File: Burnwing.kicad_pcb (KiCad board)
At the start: 2 copper layers, 54 x 22.9 mm, 43 parts, among them J1 Conn_01x06_MountingPin, J2 Molex_PicoBlade_53398-0471_1x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, J3 feather long, J4 feather short, Q1 AO3400A, U1 BTS3405GXUMA1, U1 NCV8402ADDR2G

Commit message: initial commit
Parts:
- removed +, -: SolderWirePad_1x01_SMD_1x2mm, Connector_Wire:SolderWirePad_1x01_SMD_1x2mm
- removed D4, D5: D_SOD-123F, Diode_SMD:D_SOD-123F
- removed Q1: AO3400A, Package_TO_SOT_SMD:SOT-23_Handsoldering
- removed R11: 5k1, Resistor_SMD:R_0603_1608Metric_Pad0.98x0.95mm_HandSolder
- removed the R5 at (99.3, 94.5)
- removed the R6 at (103.9, 94.5)
- added REF**: 21-0041B_8_MXM, Library:DS3231MZ_TRL-L, F.Cu at (118.5, 74.1)
- added S2: Tactile_Button, 00-footprint-lib:SW-SMD_4P-L5.1-W5.1-P3.70-LS6.5-TL-2, F.Cu at (98.7, 91.2)
- added S2: Tactile_Button, 00-footprint-lib:SW-SMD_4P-L5.1-W5.1-P3.70-LS6.5-TL-2, F.Cu at (92.3, 91.2)
- moved C2 29.6 mm to (62.9, 88.1)
- moved C3 29.6 mm to (56.7, 91.5)
- moved C4 29.6 mm to (58.2, 91.5)
- moved L1 29.6 mm to (61.3, 92.2)
- moved R1 29.6 mm to (55.2, 86.6)
- moved R2 29.6 mm to (55.2, 91.5)
- moved R7 29.6 mm to (55.2, 83.1)
- moved U1 29.6 mm to (60.5, 87.0)
- moved C1 29.6 mm to (57.6, 87.2)
- moved J1 28.5 mm to (92.8, 65.8), turned to 180 degrees
- moved D2 24.3 mm to (118.9, 105.5)
- moved D1 24.3 mm to (114.3, 105.5)
- moved R3 24.3 mm to (116.1, 105.7)
- moved R4 24.3 mm to (120.7, 105.7)
- moved Burn 1 23.1 mm to (80.4, 109.4)
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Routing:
- net GND: track 53.0 -> 3.05 mm, vias 28 -> 8
- net Vin: track 29.9 -> 1.69 mm
- net BURN_CTRL_1: track 36.0 -> 13.7 mm
- net EN3V: track 28.7 -> 7.30 mm, vias 3 -> 2
- net /Burn_Circuit/BURN_OUT_NEG: track 15.8 -> 9.24 mm
- net Net-(H3-Pad1): track 4.11 -> 0.00 mm
- net Net-(H4-Pad1): track 4.10 -> 0.00 mm
- net (no net): track 7.68 -> 3.86 mm
- net BURN_CTRL_2: track 18.6 -> 14.8 mm, vias 1 -> 0
- net Net-(H1-Pad1): track 3.59 -> 0.00 mm
- net +5V: track 2.25 -> 0.00 mm
- net IN2: track 1.92 -> 0.00 mm
- net IN1: track 1.88 -> 0.00 mm
- net /Burn_Circuit1/BURN_OUT_NEG: track 17.5 -> 15.8 mm
- removed copper zone on F.Cu, net +5V
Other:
- board size 54 x 22.9 mm -> 50.8 x 22.9 mm
- board text removed: "A4"
- board text removed: "A5"
- board text removed: "B3"
- board text removed: "B4"
- board text removed: "B5"
- board text removed: "MISO"
- board text removed: "MOSI"
- board text removed: "RX"
- board text removed: "SCK"
- board text removed: "TX"

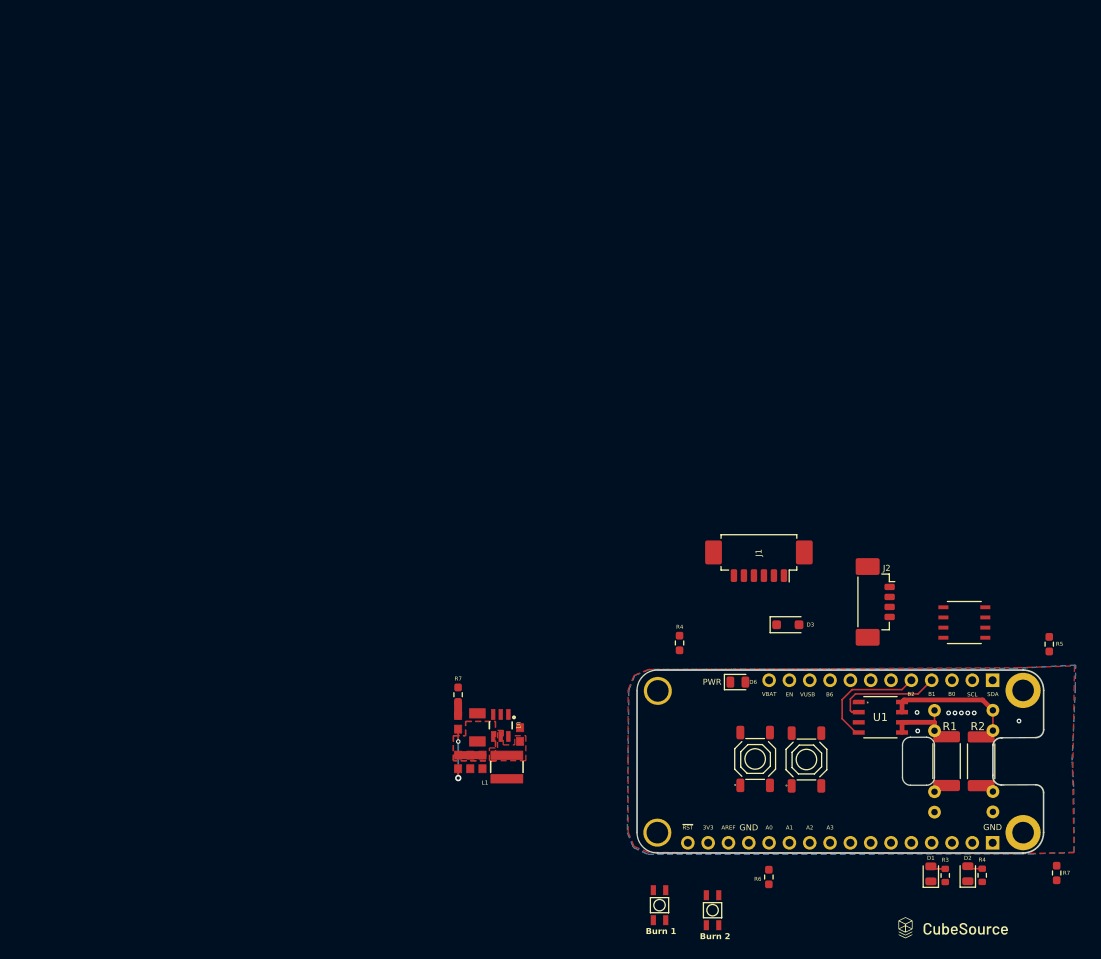
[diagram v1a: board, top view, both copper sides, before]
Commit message: Changed to USB C power
Switched our regulator for selectable usb C power delivery
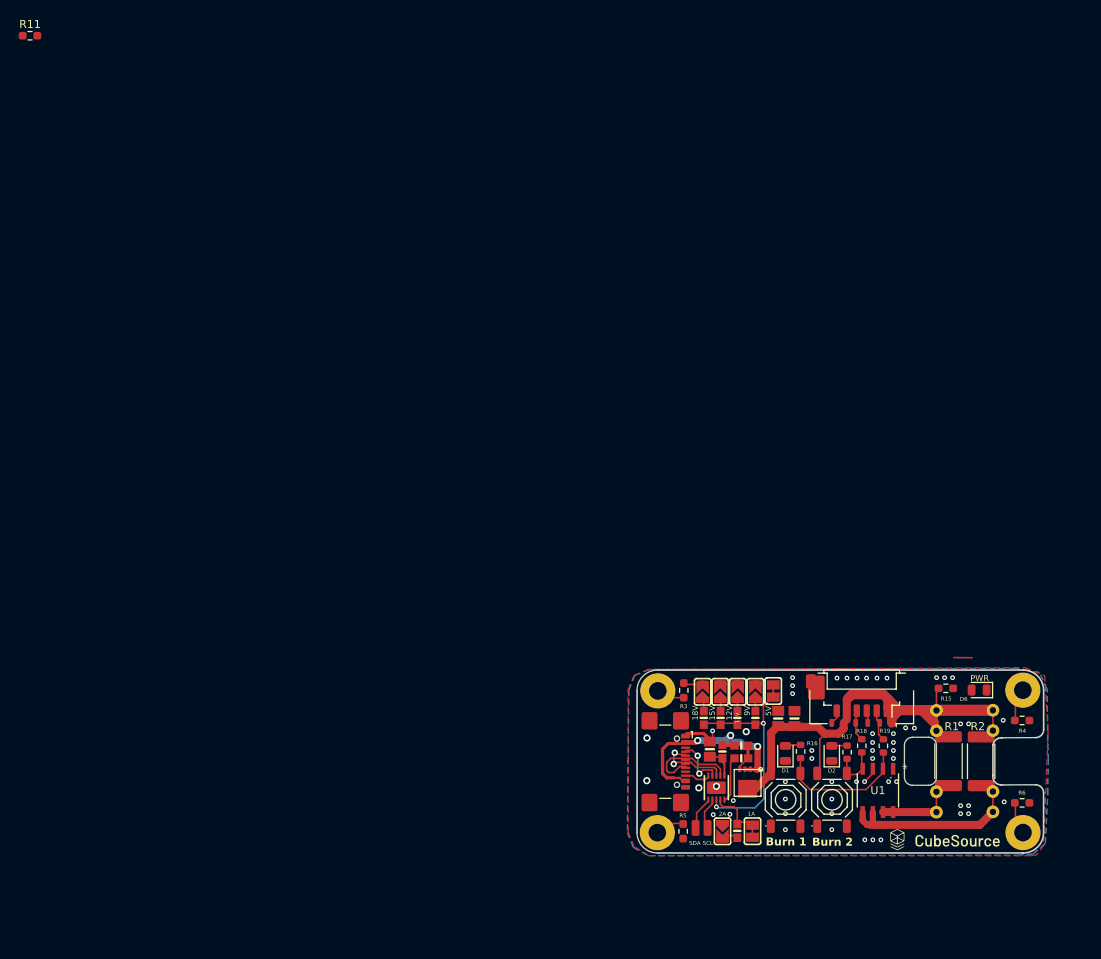
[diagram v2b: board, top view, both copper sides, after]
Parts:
- removed the Burn 1 at (80.4, 109.4)
- removed the Burn 2 at (87.0, 110.1)
- removed C1: 10uF, 1210
- removed D3: D_SOD-123F, Diode_SMD:D_SOD-123F
- removed the H3 at (125.8, 100.4)
- removed the H3 at (125.8, 82.6)
- removed J2: Molex_PicoBlade_53398-0471_1x04-1MP_P1.25mm_Vertical, Connector_Molex:Molex_PicoBlade_53398-0471_1x04-1MP_P1.25mm_Vertical
- removed J3: feather long, Connector_PinHeader_2.54mm:PinHeader_1x16_P2.54mm_Vertical
- removed J4: feather short, Connector_PinHeader_2.54mm:PinHeader_1x12_P2.54mm_Vertical
- removed L1: 4.7uH, INDUCTOR_4X4MM
- removed the R1 at (55.2, 86.6)
- removed the R2 at (55.2, 91.5)
- removed the REF** at (118.5, 74.1)
- removed the U1 at (60.5, 87.0)
- added 12V: 10K, Adafruit HUSB238 USB-C PD Breakout:0603-NO, F.Cu at (90.1, 86.0)
- added 15V: 14K, Adafruit HUSB238 USB-C PD Breakout:0603-NO, F.Cu at (88.0, 86.0)
- added 18V: 18K, Adafruit HUSB238 USB-C PD Breakout:0603-NO, F.Cu at (85.9, 86.0)
- added 1A: , Adafruit HUSB238 USB-C PD Breakout:SOLDERJUMPER_CLOSEDWIRE, F.Cu at (92.0, 100.2)
- added 2A: , Adafruit HUSB238 USB-C PD Breakout:SOLDERJUMPER_ARROW_NOPASTE, F.Cu at (88.2, 100.2)
- added 5V: , Adafruit HUSB238 USB-C PD Breakout:SOLDERJUMPER_CLOSEDWIRE, F.Cu at (94.6, 82.7)
- added 9V: 6K, Adafruit HUSB238 USB-C PD Breakout:0603-NO, F.Cu at (92.3, 86.0)
- added H2: MountingHole_Pad, MountingHole:MountingHole_2.2mm_M2_Pad, F.Cu at (125.8, 82.6)
- added H4: MountingHole_Pad, MountingHole:MountingHole_2.2mm_M2_Pad, F.Cu at (125.8, 100.4)
- added PLABEL0: , Adafruit HUSB238 USB-C PD Breakout:PLABEL0, F.Cu at (99.5, 96.2)
- added PLABEL1: , Adafruit HUSB238 USB-C PD Breakout:PLABEL1, F.Cu at (89.7, 106.1)
- added PLABEL10: , Adafruit HUSB238 USB-C PD Breakout:PLABEL10, F.Cu at (95.5, 86.2)
- added PLABEL12: , Adafruit HUSB238 USB-C PD Breakout:PLABEL12, F.Cu at (89.5, 97.2)
- added PLABEL13: , Adafruit HUSB238 USB-C PD Breakout:PLABEL13, F.Cu at (85.2, 97.2)
- added PLABEL14: , Adafruit HUSB238 USB-C PD Breakout:PLABEL14, F.Cu at (83.0, 97.2)
- added PLABEL15: , Adafruit HUSB238 USB-C PD Breakout:PLABEL15, F.Cu at (82.8, 99.5)
- added PLABEL16: , Adafruit HUSB238 USB-C PD Breakout:PLABEL16, F.Cu at (99.5, 93.8)
- added PLABEL17: , Adafruit HUSB238 USB-C PD Breakout:PLABEL17, F.Cu at (101.6, 89.0)
- added PLABEL18: , Adafruit HUSB238 USB-C PD Breakout:PLABEL18, B.Cu at (81.0, 91.3)
- added PLABEL19: , Adafruit HUSB238 USB-C PD Breakout:PLABEL19, B.Cu at (88.8, 91.3)
- added PLABEL2: , Adafruit HUSB238 USB-C PD Breakout:PLABEL2, F.Cu at (92.2, 108.7)
- added PLABEL3: , Adafruit HUSB238 USB-C PD Breakout:PLABEL3, F.Cu at (99.5, 98.8)
- added PLABEL4: , Adafruit HUSB238 USB-C PD Breakout:PLABEL4, F.Cu at (85.1, 91.7)
- added PLABEL8: , Adafruit HUSB238 USB-C PD Breakout:PLABEL8, F.Cu at (91.6, 86.2)
- added PLABEL9: , Adafruit HUSB238 USB-C PD Breakout:PLABEL9, F.Cu at (94.0, 86.2)
- added Q1: AONR21307, Adafruit HUSB238 USB-C PD Breakout:POWERDI3333, F.Cu at (91.4, 93.9)
- added R11: 6K, Resistor_SMD:R_0603_1608Metric_Pad0.98x0.95mm_HandSolder, F.Cu at (1.68, 0.76)
- added R15: 6K, Resistor_SMD:R_0603_1608Metric_Pad0.98x0.95mm_HandSolder, F.Cu at (116.2, 82.3)
- added R18: 5.1K, Resistor_SMD:R_0603_1608Metric, F.Cu at (105.7, 89.5)
- added R19: 14K, Resistor_SMD:R_0603_1608Metric, F.Cu at (108.3, 89.5)
- added R8: 49.9K, Adafruit HUSB238 USB-C PD Breakout:0603-NO, F.Cu at (90.1, 100.1)
- added R8: 49.9K, Adafruit HUSB238 USB-C PD Breakout:0603-NO, F.Cu at (90.6, 89.5)
- added R9: 5.1K, Adafruit HUSB238 USB-C PD Breakout:0603-NO, F.Cu at (90.6, 91.1)
- added SCL: SolderWirePad_1x01_SMD_1x2mm, Library:SolderWirePad_1x01_SMD_1x2mm, F.Cu at (86.4, 99.8)
- added SDA: SolderWirePad_1x01_SMD_1x2mm, Library:SolderWirePad_1x01_SMD_1x2mm, F.Cu at (84.9, 99.8)
- added SJ2: SOLDERJUMPER, Adafruit HUSB238 USB-C PD Breakout:SOLDERJUMPER_ARROW_NOPASTE, F.Cu at (92.3, 82.8)
- added SJ3: SOLDERJUMPER, Adafruit HUSB238 USB-C PD Breakout:SOLDERJUMPER_ARROW_NOPASTE, F.Cu at (90.2, 82.8)
- added SJ4: SOLDERJUMPER, Adafruit HUSB238 USB-C PD Breakout:SOLDERJUMPER_ARROW_NOPASTE, F.Cu at (88.0, 82.8)
- added SJ5: SOLDERJUMPER, Adafruit HUSB238 USB-C PD Breakout:SOLDERJUMPER_ARROW_NOPASTE, F.Cu at (85.8, 82.8)
- added X1: USB_C_Receptacle_GCT_USB4110, Connector_USB:USB_C_Receptacle_GCT_USB4110, F.Cu at (79.9, 91.5)
- added X3: HUSB238, Adafruit HUSB238 USB-C PD Breakout:DFN10_3X3MM, F.Cu at (87.5, 94.8)
- added p: Molex_Pico-Lock_504050-0691_1x06-1MP_P1.50mm_Horizontal, Connector_Molex:Molex_Pico-Lock_504050-0691_1x06-1MP_P1.50mm_Horizontal, F.Cu at (105.6, 83.9)
- Burn 1: renamed from S2
- Burn 2: renamed from S2
- C2: value 0.1uF -> 100n; footprint 0603 -> Adafruit HUSB238 USB-C PD Breakout:0805-NO
- C3: value 0.1uF -> 1uF/50V; footprint 0603 -> Adafruit HUSB238 USB-C PD Breakout:0805-NO
- C4: value 22uF -> 4.7uF; footprint 0603 -> Adafruit HUSB238 USB-C PD Breakout:0805-NO
- G***: footprint LOGO -> Library:LOGO
- R1: value R -> 4.7
- R16: renamed from R3; value 10 -> 10 ohm
- R17: renamed from R4; value 10 -> 49.9K
- R2: value AxialBurnResistor_No_Cutout -> 4.7
- R7: value 0 -> 10 ohm; footprint Resistor_SMD:R_0603_1608Metric_Pad0.98x0.95mm_HandSolder -> Adafruit HUSB238 USB-C PD Breakout:0603-NO
- moved C4 39.4 mm to (97.2, 86.1)
- moved R7 33.8 mm to (88.2, 90.2), turned to 90 degrees
- moved C2 32.3 mm to (95.2, 86.1), turned to 90 degrees
- moved D6 30.2 mm to (120.3, 82.5), turned to 180 degrees
- moved C3 30.0 mm to (86.7, 89.9)
- moved R16 23.8 mm to (98.0, 90.2)
- moved D1 23.6 mm to (96.1, 90.5)
- moved R17 22.8 mm to (103.8, 90.3)
- moved D2 22.7 mm to (101.9, 90.5)
- moved J1 21.2 mm to (105.6, 82.7)
- moved R5 12.1 mm to (83.3, 100.2)
- moved G*** 11.1 mm to (116.0, 101.3)
- moved Burn 2 10.9 mm to (101.9, 96.3)
- moved R4 10.1 mm to (125.7, 86.3), turned to 0 degrees
- moved R6 9.77 mm to (125.7, 96.6), turned to 0 degrees
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- renumbered R4 to R3, R5 to R4, R6 to R5, R7 to R6
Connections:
- Burn 1 pad 1: (no net) -> VOUT
- Burn 1 pad 2: (no net) -> VOUT
- Burn 1 pad 3: (no net) -> BURN_CTRL_1
- Burn 1 pad 4: (no net) -> BURN_CTRL_1
- Burn 2 pad 1: (no net) -> VOUT
- Burn 2 pad 2: (no net) -> VOUT
- Burn 2 pad 3: (no net) -> BURN_CTRL_1
- Burn 2 pad 4: (no net) -> BURN_CTRL_2
- C2 pad 1: (no net) -> VDC
- C2 pad 2: Vin -> GND
- C3 pad 1: +5V -> Net-(X3-VIN)
- C4 pad 1: +5V -> /VOUT
- D6 pad 2: Vin -> (no net)
- J1 pad 1: Vin -> VOUT
- J1 pad 2: Vin -> BURN_CTRL_1
- J1 pad 3: Vin -> GND
- J1 pad 4: GND -> BURN_CTRL_2
- J1 pad 5: GND -> VOUT
- R1 pad 1: /Burn_Circuit/BURN_OUT_NEG -> unconnected-(R1-Pad1)
- R1 pad 2: +5V -> Net-(R1-Pad2)
- R16 pad 1: IN1 -> Net-(X3-VIN)
- R16 pad 2: (no net) -> Net-(Q1-S-Pad1)
- R17 pad 1: IN2 -> Net-(Q1-S-Pad1)
- R17 pad 2: (no net) -> Net-(Q1-G)
- R2 pad 1: /Burn_Circuit1/BURN_OUT_NEG -> unconnected-(R2-Pad1)
- R2 pad 2: +5V -> Net-(R2-Pad2)
- R4 pad 1: (no net) -> Net-(H2-Pad1)
- R5 pad 1: GND -> Net-(H3-Pad1)
- R5 pad 2: Net-(H3-Pad1) -> GND
- R7 pad 1: Vin -> Net-(X3-VIN)
- R7 pad 2: Vin -> Net-(Q1-S-Pad1)
- REF** pad 1: /Burn_Circuit1/BURN_OUT_NEG -> VOUT
- REF** pad 2: +5V -> Net-(R2-Pad2)
- REF** pad 1: /Burn_Circuit/BURN_OUT_NEG -> VOUT
- REF** pad 2: +5V -> Net-(R1-Pad2)
- U1 pad 1: GND -> unconnected-(U1-SOURCE1-Pad1)
- U1 pad 2: BURN_CTRL_1 -> /GATE1
- U1 pad 3: GND -> unconnected-(U1-SOURCE2-Pad3)
- U1 pad 4: BURN_CTRL_2 -> /GATE2
- U1 pad 5: /Burn_Circuit/BURN_OUT_NEG -> Net-(R2-Pad2)
- U1 pad 6: /Burn_Circuit/BURN_OUT_NEG -> Net-(R2-Pad2)
- U1 pad 7: /Burn_Circuit1/BURN_OUT_NEG -> Net-(R1-Pad2)
- U1 pad 8: /Burn_Circuit1/BURN_OUT_NEG -> Net-(R1-Pad2)
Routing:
- net VOUT: track 0.00 -> 78.6 mm
- net Net-(Q1-S-Pad1): track 0.00 -> 30.5 mm, vias 0 -> 2
- net N$3: track 0.00 -> 27.9 mm, vias 0 -> 2
- net Net-(R2-Pad2): track 0.00 -> 22.5 mm
- net /Burn_Circuit1/BURN_OUT_NEG: track 15.8 -> 0.00 mm
- net /D+: track 0.00 -> 12.3 mm
- net GND: track 3.05 -> 13.5 mm, vias 8 -> 56
- net /D-: track 0.00 -> 9.69 mm, vias 0 -> 2
- net /Burn_Circuit/BURN_OUT_NEG: track 9.24 -> 0.00 mm
- net Net-(R1-Pad2): track 0.00 -> 9.01 mm
- net EN3V: track 7.30 -> 0.00 mm, vias 2 -> 0
- net BURN_CTRL_1: track 13.7 -> 21.0 mm
- net /CC1: track 0.00 -> 6.75 mm, vias 0 -> 2
- net N$9: track 0.00 -> 6.19 mm
- net Net-(X3-GATE): track 0.00 -> 5.83 mm
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- removed copper zone on F.Cu, net Vin
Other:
- board text removed: "3V3"
- board text removed: "A0"
- board text removed: "A1"
- board text removed: "A2"
- board text removed: "A3"
- board text removed: "AREF"
- board text removed: "B0"
- board text removed: "B1"
- board text removed: "B2"
- board text removed: "B6"
- board text removed: "EN"
- board text removed: "GND"
- board text removed: "SCL"
- board text removed: "SDA"
- board text removed: "VBAT"
- board text removed: "VUSB"
- board text removed: "~{RST}"

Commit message: updated layou/schematic
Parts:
- removed the 12V at (90.1, 86.0)
- removed the 15V at (88.0, 86.0)
- removed the 18V at (85.9, 86.0)
- removed 1A: , Adafruit HUSB238 USB-C PD Breakout:SOLDERJUMPER_CLOSEDWIRE
- removed 2A: , Adafruit HUSB238 USB-C PD Breakout:SOLDERJUMPER_ARROW_NOPASTE
- removed the 9V at (92.3, 86.0)
- removed PLABEL1: , Adafruit HUSB238 USB-C PD Breakout:PLABEL1
- removed PLABEL12: , Adafruit HUSB238 USB-C PD Breakout:PLABEL12
- removed PLABEL13: , Adafruit HUSB238 USB-C PD Breakout:PLABEL13
- removed PLABEL15: , Adafruit HUSB238 USB-C PD Breakout:PLABEL15
- removed PLABEL19: , Adafruit HUSB238 USB-C PD Breakout:PLABEL19
- removed PLABEL2: , Adafruit HUSB238 USB-C PD Breakout:PLABEL2
- removed R11: 6K, Resistor_SMD:R_0603_1608Metric_Pad0.98x0.95mm_HandSolder
- removed R18: 5.1K, Resistor_SMD:R_0603_1608Metric
- removed R19: 14K, Resistor_SMD:R_0603_1608Metric
- removed the R8 at (90.1, 100.1)
- removed the R8 at (90.6, 89.5)
- removed R9: 5.1K, Adafruit HUSB238 USB-C PD Breakout:0603-NO
- removed SCL, SDA: SolderWirePad_1x01_SMD_1x2mm, Library:SolderWirePad_1x01_SMD_1x2mm
- removed SJ2, SJ3, SJ4, SJ5: SOLDERJUMPER, Adafruit HUSB238 USB-C PD Breakout:SOLDERJUMPER_ARROW_NOPASTE
- added 12V: , Adafruit HUSB238 USB-C PD Breakout:SOLDERJUMPER_ARROW_NOPASTE, F.Cu at (88.5, 82.8)
- added 15V: , Adafruit HUSB238 USB-C PD Breakout:SOLDERJUMPER_ARROW_NOPASTE, F.Cu at (86.2, 82.8)
- added 18V: , Adafruit HUSB238 USB-C PD Breakout:SOLDERJUMPER_ARROW_NOPASTE, F.Cu at (84.0, 82.8)
- added 9V: , Adafruit HUSB238 USB-C PD Breakout:SOLDERJUMPER_ARROW_NOPASTE, F.Cu at (90.7, 82.8)
- added C1: 1uF/50V, Adafruit HUSB238 USB-C PD Breakout:0805-NO, F.Cu at (86.8, 90.1)
- added PLABEL11: , Adafruit HUSB238 USB-C PD Breakout:PLABEL11, F.Cu at (87.3, 91.0)
- added PLABEL5: , Adafruit HUSB238 USB-C PD Breakout:PLABEL5, F.Cu at (84.1, 85.0)
- added PLABEL6: , Adafruit HUSB238 USB-C PD Breakout:PLABEL6, F.Cu at (86.5, 85.1)
- added PLABEL7: , Adafruit HUSB238 USB-C PD Breakout:PLABEL7, F.Cu at (88.8, 85.5)
- added R1: 6K, Adafruit HUSB238 USB-C PD Breakout:0603-NO, F.Cu at (91.3, 86.2)
- added R2: 10K, Adafruit HUSB238 USB-C PD Breakout:0603-NO, F.Cu at (89.3, 86.2)
- added R4: 5.1K, Adafruit HUSB238 USB-C PD Breakout:0603-NO, F.Cu at (90.0, 93.7)
- added R6: 14K, Adafruit HUSB238 USB-C PD Breakout:0603-NO, F.Cu at (87.3, 86.2)
- added R8: 14K, Adafruit HUSB238 USB-C PD Breakout:0603-NO, F.Cu at (86.6, 100.0)
- added SJ6: , Adafruit HUSB238 USB-C PD Breakout:SOLDERJUMPER_CLOSEDWIRE, F.Cu at (88.5, 99.9)
- added SJ7: , Adafruit HUSB238 USB-C PD Breakout:SOLDERJUMPER_ARROW_NOPASTE, F.Cu at (84.7, 100.0)
- Burn1: renamed from Burn 1
- Burn2: renamed from Burn 2
- C2: value 100n -> 4.7uF
- C3: value 1uF/50V -> 4.7uF
- R16: value 10 ohm -> 150; footprint Resistor_SMD:R_0603_1608Metric -> Adafruit HUSB238 USB-C PD Breakout:0603-NO
- R17: value 49.9K -> 150; footprint Resistor_SMD:R_0603_1608Metric -> Adafruit HUSB238 USB-C PD Breakout:0603-NO
- R3: value 0 -> 10 ohm; footprint Resistor_SMD:R_0603_1608Metric_Pad0.98x0.95mm_HandSolder -> Adafruit HUSB238 USB-C PD Breakout:0603-NO
- R5: value 0 -> 49.9K; footprint Resistor_SMD:R_0603_1608Metric_Pad0.98x0.95mm_HandSolder -> Adafruit HUSB238 USB-C PD Breakout:0603-NO
- R7: value 10 ohm -> 18K
- X1: value USB_C_Receptacle_GCT_USB4110 -> USB Type C; footprint Connector_USB:USB_C_Receptacle_GCT_USB4110 -> Adafruit HUSB238 USB-C PD Breakout:USB_C_CUSB31-CFM2AX-01-X
- moved R5 11.7 mm to (89.9, 90.5)
- moved PLABEL10 11.6 mm to (87.3, 94.4)
- moved PLABEL9 11.6 mm to (85.7, 94.4)
- moved C3 11.1 mm to (96.2, 84.2), turned to 0 degrees
- moved D1 9.61 mm to (105.7, 91.3), turned to -90 degrees
- moved R3 9.34 mm to (88.4, 90.5)
- moved R16 5.93 mm to (103.8, 91.3), turned to -90 degrees
- moved D2 5.93 mm to (107.8, 91.3), turned to -90 degrees
- moved R17 5.91 mm to (109.6, 91.3), turned to -90 degrees
- moved Q1 5.25 mm to (94.2, 89.5), turned to 0 degrees
- moved R7 4.99 mm to (85.3, 86.2), turned to -90 degrees
- moved PLABEL8 4.30 mm to (93.5, 90.1)
- moved C4 4.12 mm to (96.2, 82.1), turned to 0 degrees
- moved Burn1 2.37 mm to (93.8, 95.6)
- moved Burn2 2.11 mm to (99.9, 95.6)
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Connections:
- net /CC1 renamed CC1
- net /CC2 renamed CC2
- net /D+ renamed D+
- net /D- renamed D-
- Burn2 pad 3: BURN_CTRL_1 -> BURN_CTRL_2
- C2 pad 1: VDC -> VOUT
- C3 pad 1: Net-(X3-VIN) -> VOUT
- C4 pad 1: /VOUT -> VOUT
- D1 pad 1: GND -> (no net)
- D2 pad 1: GND -> (no net)
- D6 pad 1: GND -> Net-(X3-VIN)
- Q1 pad 1: Net-(Q1-S-Pad1) -> VBUS
- Q1 pad 2: Net-(Q1-S-Pad1) -> VBUS
- Q1 pad 3: Net-(Q1-S-Pad1) -> VBUS
- Q1 pad 4: Net-(Q1-G) -> N$2
- Q1 pad 5678: /VOUT -> VOUT
- R1 pad 1: unconnected-(R1-Pad1) -> VOUT
- R16 pad 1: Net-(X3-VIN) -> (no net)
- R16 pad 2: Net-(Q1-S-Pad1) -> (no net)
- R17 pad 1: Net-(Q1-S-Pad1) -> (no net)
- R17 pad 2: Net-(Q1-G) -> (no net)
- R2 pad 1: unconnected-(R2-Pad1) -> VOUT
- R3 pad 1: Net-(H1-Pad1) -> N$1
- R3 pad 2: GND -> VBUS
- R5 pad 1: Net-(H3-Pad1) -> VBUS
- R5 pad 2: GND -> N$2
- R7 pad 1: Net-(X3-VIN) -> N$8
- R7 pad 2: Net-(Q1-S-Pad1) -> N$3
- U1 pad 1: unconnected-(U1-SOURCE1-Pad1) -> GND
- U1 pad 3: unconnected-(U1-SOURCE2-Pad3) -> GND
- X1 pad A8: unconnected-(X1-SBU1-PadA8) -> (no net)
- X1 pad B8: unconnected-(X1-SBU2-PadB8) -> (no net)
- X3 pad 1: Net-(X3-VIN) -> N$1
- X3 pad 6: /SDA -> SDA
- X3 pad 7: /SCL -> SCL
- X3 pad 8: Net-(X3-VSET) -> N$3
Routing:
- net Net-(Q1-S-Pad1): track 30.5 -> 0.00 mm, vias 2 -> 0
- net VOUT: track 78.6 -> 52.0 mm
- net VBUS: track 0.00 -> 21.5 mm, vias 0 -> 2
- net BURN_CTRL_1: track 21.0 -> 1.84 mm
- net BURN_CTRL_2: track 10.1 -> 1.74 mm
- net N$9 (its old number): track 6.19 -> 0.00 mm
- net Net-(R2-Pad2): track 22.5 -> 16.9 mm
- net Net-(Q1-G): track 5.43 -> 0.00 mm
- net Net-(H3-Pad1): track 5.43 -> 0.00 mm
- net GND: track 13.5 -> 18.7 mm, vias 56 -> 32
- net Net-(R1-Pad2): track 9.01 -> 14.1 mm
- net /SCL: track 4.99 -> 0.00 mm
- net N$2: track 0.00 -> 4.74 mm
- net N$9: track 0.00 -> 4.72 mm
- net /SDA: track 4.42 -> 0.00 mm
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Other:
- outline, holes or cut-outs redrawn
